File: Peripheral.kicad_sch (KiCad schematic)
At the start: 3 parts, among them U2 AT24CS02-XHM, U3 ICM-20602, U4 TJA1051T

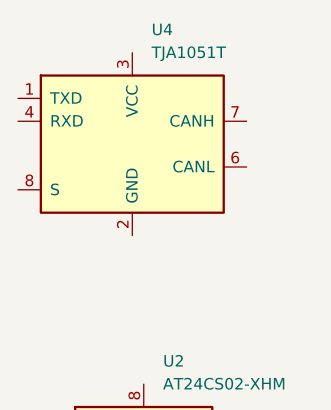
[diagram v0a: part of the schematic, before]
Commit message: 增加ADC采样，优化PWM
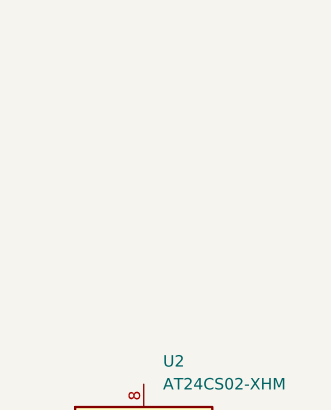
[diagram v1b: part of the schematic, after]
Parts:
- removed U4: TJA1051T, Package_SO:SOIC-8_3.9x4.9mm_P1.27mm, symbol Interface_CAN_LIN:TJA1051T
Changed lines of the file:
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@@
-	)
-	(symbol
-		(lib_id "Interface_CAN_LIN:TJA1051T")
-		(at 74.93 57.15 0)
-		(unit 1)
-		(exclude_from_sim no)
-		(in_bom yes)
-		(on_board yes)
-		(dnp no)
-		(fields_autoplaced yes)
-		(property "Reference" "U4"
-			(at 77.0733 44.45 0)
-			(effects
-				(font
-					(size 1.27 1.27)
-				)
-				(justify left)
-			)
-		)
-		(property "Value" "TJA1051T"
-			(at 77.0733 46.99 0)
-			(effects
-				(font
-					(size 1.27 1.27)
-				)
-				(justify left)
-			)
-		)
-		(property "Footprint" "Package_SO:SOIC-8_3.9x4.9mm_P1.27mm"
-			(at 74.93 69.85 0)
-			(effects
-				(font
-					(size 1.27 1.27)
-					(italic yes)
-				)
-				(hide yes)
-			)
-		)
-		(property "Datasheet" "http://www.nxp.com/docs/en/data-sheet/TJA1051.pdf"
-			(at 74.93 57.15 0)
-			(effects
-				(font
-					(size 1.27 1.27)
-				)
-				(hide yes)
-			)
-		)
-		(property "Description" "High-Speed CAN Transceiver, silent mode, SOIC-8"
-			(at 74.93 57.15 0)
-			(effects
-				(font
-					(size 1.27 1.27)
-				)
-				(hide yes)
-			)
-		)
-		(pin "6"
-		)
-		(pin "2"
-		)
-		(pin "1"
-		)
-		(pin "4"
-		)
-		(pin "5"
-		)
-		(pin "3"
-		)
-		(pin "8"
-		)
-		(pin "7"
-		)
-		(instances
-			(project "ControlBoard"
-				(path "/bfd4cee4-1f26-4ec9-a630-f44d434f4dbf/abd141e4-a687-4ce0-a8e9-dc522ad2ef55/5828d2be-30cc-492b-81f0-4c9eb7634256"
-					(reference "U4")
-					(unit 1)
-				)
-			)
-		)
 	)
 	(symbol

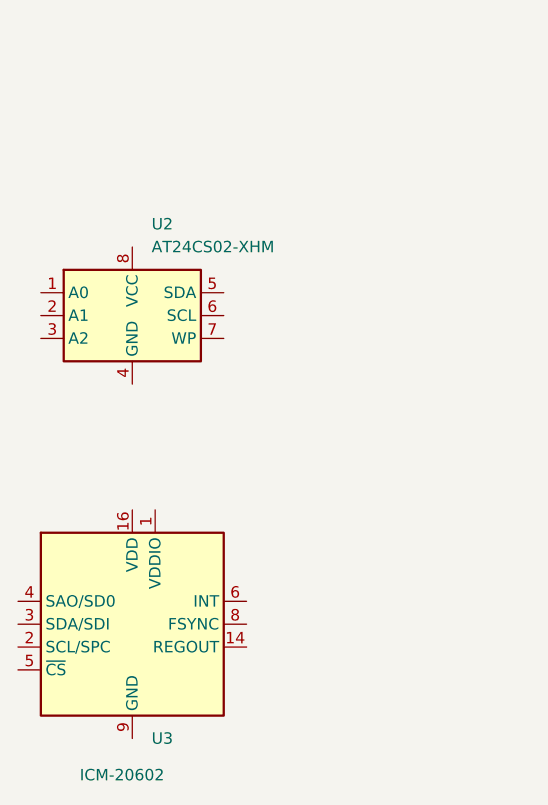
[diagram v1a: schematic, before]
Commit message: 完成部分I2C/FDCAN引脚分配
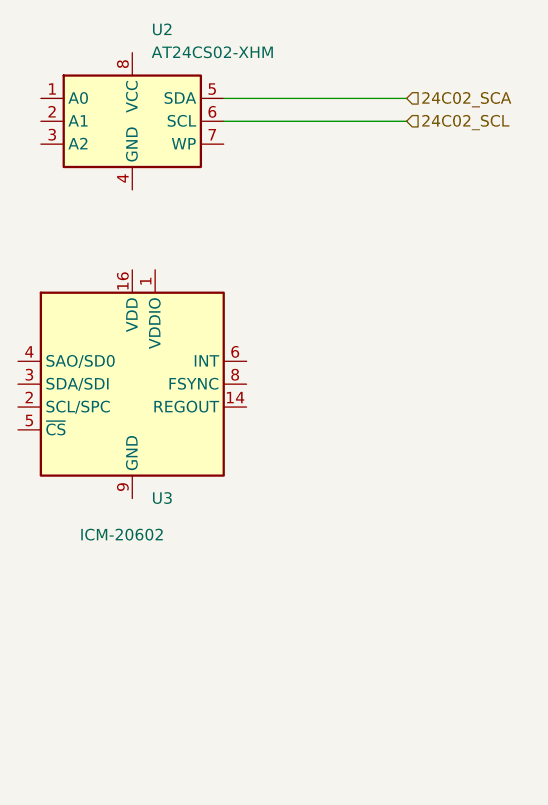
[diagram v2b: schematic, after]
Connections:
- net 24C02_SCA: now reaches U2.5 (SDA)
- net 24C02_SCL: now reaches U2.6 (SCL)
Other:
- moved on the sheet: U2, U3
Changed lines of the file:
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@@
 	(generator_version "9.0")
 	(paper "A4")
+	(wire
+		(pts
+			(xy 86.36 69.85) (xy 106.68 69.85)
+		)
+		(stroke
+			(width 0)
+			(type default)
+		)
+	)
+	(wire
+		(pts
+			(xy 86.36 67.31) (xy 106.68 67.31)
+		)
+		(stroke
+			(width 0)
+			(type default)
+		)
+	)
+	(hierarchical_label "24C02_SCL"
+		(shape input)
+		(at 106.68 69.85 0)
+		(effects
+			(font
+				(size 1.27 1.27)
+			)
+			(justify left)
+		)
+	)
+	(hierarchical_label "24C02_SCA"
+		(shape input)
+		(at 106.68 67.31 0)
+		(effects
+			(font
+				(size 1.27 1.27)
+			)
+			(justify left)
+		)
+	)
 	(symbol
 		(lib_id "Memory_EEPROM:AT24CS02-XHM")
-		(at 76.2 91.44 0)
+		(at 76.2 69.85 0)
 		(unit 1)
 		(exclude_from_sim no)
@@
 		(fields_autoplaced yes)
 		(property "Reference" "U2"
-			(at 78.3433 81.28 0)
+			(at 78.3433 59.69 0)
 			(effects
 				(font
@@
 		)
 		(property "Value" "AT24CS02-XHM"
-			(at 78.3433 83.82 0)
+			(at 78.3433 62.23 0)
 			(effects
 				(font
@@
 		)
 		(property "Footprint" "Package_SO:TSSOP-8_4.4x3mm_P0.65mm"
-			(at 76.2 91.44 0)
+			(at 76.2 69.85 0)
 			(effects
 				(font
@@
 		)
 		(property "Datasheet" "http://ww1.microchip.com/downloads/en/DeviceDoc/Atmel-8815-SEEPROM-AT24CS01-02-Datasheet.pdf"
-			(at 76.2 91.44 0)
+			(at 76.2 69.85 0)
 			(effects
 				(font
@@
 		)
 		(property "Description" "I2C Serial EEPROM, 2Kb (256x8) with Unique Serial Number, TSSOP8"
-			(at 76.2 91.44 0)
+			(at 76.2 69.85 0)
 			(effects
 				(font
@@
 	(symbol
 		(lib_id "Sensor_Motion:ICM-20602")
-		(at 76.2 125.73 0)
+		(at 76.2 99.06 0)
 		(unit 1)
 		(exclude_from_sim no)
@@
 		(dnp no)
 		(property "Reference" "U3"
-			(at 78.3433 138.43 0)
+			(at 78.3433 111.76 0)
 			(effects
 				(font
@@
 		)
 		(property "Value" "ICM-20602"
-			(at 70.358 142.494 0)
+			(at 70.358 115.824 0)
 			(effects
 				(font
@@
 		)
 		(property "Footprint" "Package_LGA:LGA-16_3x3mm_P0.5mm_LayoutBorder3x5y"
-			(at 76.2 119.38 0)
+			(at 76.2 92.71 0)
 			(effects
 				(font
@@
 		)
 		(property "Datasheet" "http://www.invensense.com/wp-content/uploads/2016/10/DS-000176-ICM-20602-v1.0.pdf"
-			(at 77.47 101.6 0)
+			(at 77.47 74.93 0)
 			(effects
 				(font
@@
 		)
 		(property "Description" "High performance 6-Axis MEMS motion tracking, SPI/I2C interface, LGA-16"
-			(at 76.2 125.73 0)
+			(at 76.2 99.06 0)
 			(effects
 				(font

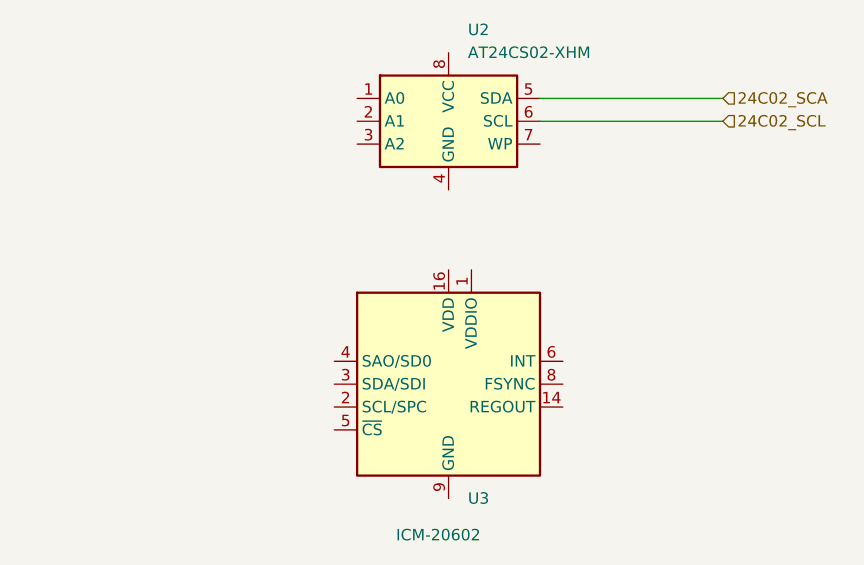
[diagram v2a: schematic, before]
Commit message: 增加3.3V电路
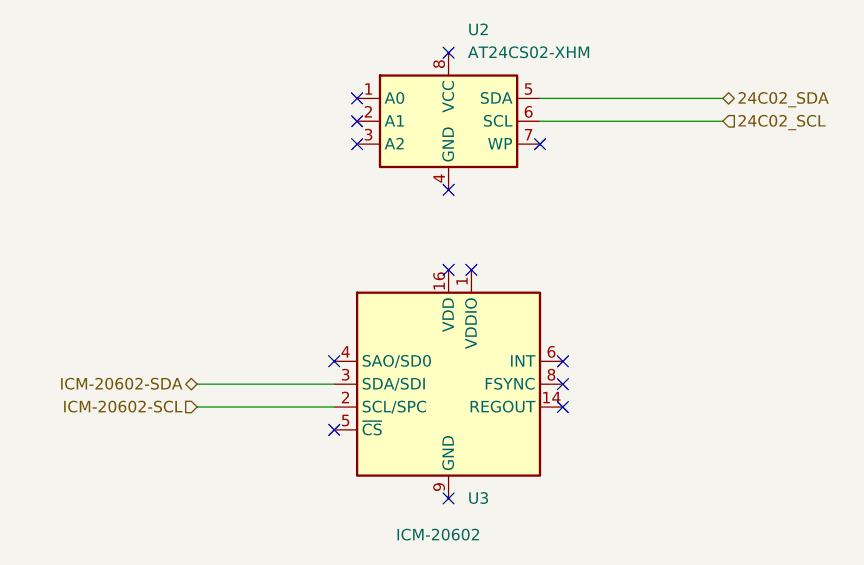
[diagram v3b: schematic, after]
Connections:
- net ICM-20602-SCL: now reaches U3.2 (SCL/SPC)
- net ICM-20602-SDA: now reaches U3.3 (SDA/SDI)
- net 24C02_SCA renamed 24C02_SDA
- no-connect marks 0 -> 14
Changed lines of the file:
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@@
 	(generator_version "9.0")
 	(paper "A4")
+	(no_connect
+		(at 63.5 96.52)
+	)
+	(no_connect
+		(at 88.9 99.06)
+	)
+	(no_connect
+		(at 66.04 72.39)
+	)
+	(no_connect
+		(at 78.74 86.36)
+	)
+	(no_connect
+		(at 63.5 104.14)
+	)
+	(no_connect
+		(at 66.04 67.31)
+	)
+	(no_connect
+		(at 88.9 101.6)
+	)
+	(no_connect
+		(at 88.9 96.52)
+	)
+	(no_connect
+		(at 66.04 69.85)
+	)
+	(no_connect
+		(at 86.36 72.39)
+	)
+	(no_connect
+		(at 76.2 111.76)
+	)
+	(no_connect
+		(at 76.2 62.23)
+	)
+	(no_connect
+		(at 76.2 77.47)
+	)
+	(no_connect
+		(at 76.2 86.36)
+	)
+	(wire
+		(pts
+			(xy 48.26 99.06) (xy 63.5 99.06)
+		)
+		(stroke
+			(width 0)
+			(type default)
+		)
+	)
+	(wire
+		(pts
+			(xy 48.26 101.6) (xy 63.5 101.6)
+		)
+		(stroke
+			(width 0)
+			(type default)
+		)
+	)
 	(wire
 		(pts
@@
 		)
 	)
+	(hierarchical_label "ICM-20602-SDA"
+		(shape bidirectional)
+		(at 48.26 99.06 180)
+		(effects
+			(font
+				(size 1.27 1.27)
+			)
+			(justify right)
+		)
+	)
 	(hierarchical_label "24C02_SCL"
 		(shape input)
@@
 		)
 	)
-	(hierarchical_label "24C02_SCA"
-		(shape input)
+	(hierarchical_label "24C02_SDA"
+		(shape bidirectional)
 		(at 106.68 67.31 0)
 		(effects
@@
 		)
 	)
+	(hierarchical_label "ICM-20602-SCL"
+		(shape input)
+		(at 48.26 101.6 180)
+		(effects
+			(font
+				(size 1.27 1.27)
+			)
+			(justify right)
+		)
+	)

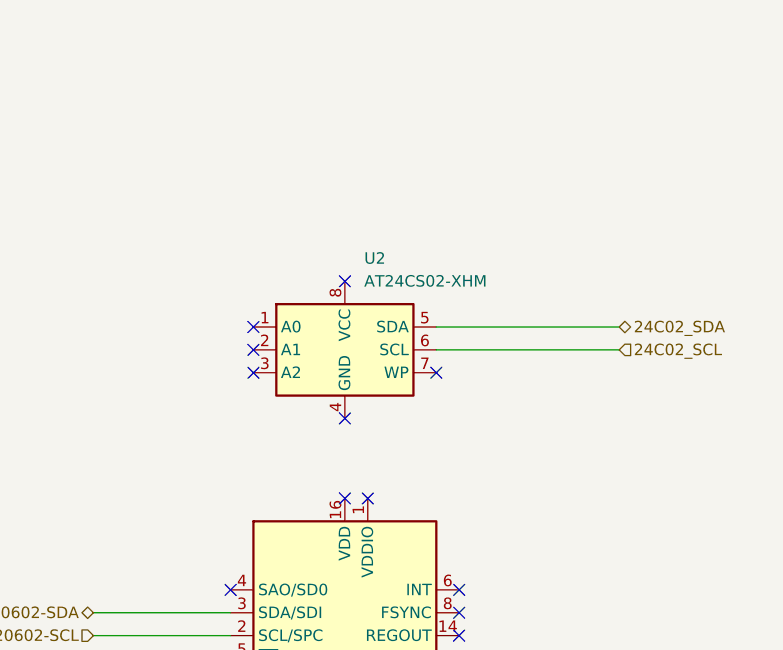
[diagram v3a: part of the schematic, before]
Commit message: 优化EEPROM电路
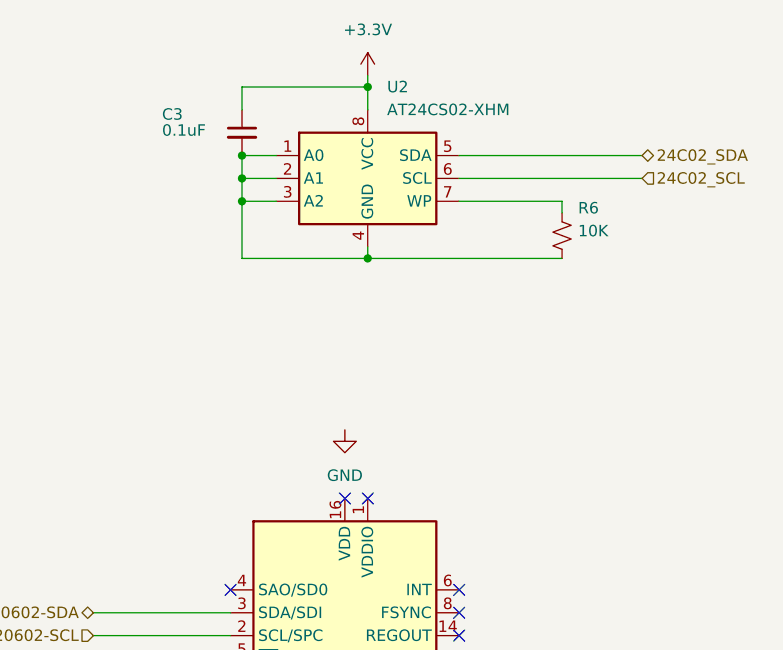
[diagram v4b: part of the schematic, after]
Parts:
- added C3: 0.1uF, symbol Device:C_Small
- added R6: 10K, symbol Device:R_Small_US
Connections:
- net at U2.1 (A0): now also U2.2 (A1), U2.3 (A2), U2.4 (GND), C3.2, R6.2
- net at U2.7 (WP): now also R6.1
- net +3.3V: now reaches U2.8 (VCC)
- net +3.3V: now also C3.1
- no-connect marks 14 -> 8
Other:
- moved on the sheet: U2

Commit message: 优化IMU电路
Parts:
- added U6: ICM-4268-P, Package_LGA:Bosch_LGA-14_3x2.5mm_P0.5mm, symbol User_Driver:ICM-42688-P
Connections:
- net GND: now also C3.2, R6.2, U2.1 (A0), U2.2 (A1), U2.3 (A2), U2.4 (GND)
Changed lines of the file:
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@@
 	(symbol
 		(lib_id "power:GND")
-		(at 76.2 78.74 0)
+		(at 78.74 59.69 0)
 		(unit 1)
 		(exclude_from_sim no)
@@
 		(fields_autoplaced yes)
 		(property "Reference" "#PWR012"
-			(at 76.2 85.09 0)
+			(at 78.74 66.04 0)
 			(effects
 				(font
@@
 		)
 		(property "Value" "GND"
-			(at 76.2 83.82 0)
+			(at 78.74 64.77 0)
 			(effects
 				(font
@@
 		)
 		(property "Footprint" ""
-			(at 76.2 78.74 0)
+			(at 78.74 59.69 0)
 			(effects
 				(font
@@
 		)
 		(property "Datasheet" ""
-			(at 76.2 78.74 0)
+			(at 78.74 59.69 0)
 			(effects
 				(font
@@
 		)
 		(property "Description" "Power symbol creates a global label with name \"GND\" , ground"
-			(at 76.2 78.74 0)
+			(at 78.74 59.69 0)
 			(effects
 				(font
@@
 					(unit 1)
 				)
+			)
+		)
+	)
+	(symbol
+		(lib_id "User_Driver:ICM-42688-P")
+		(at 113.03 85.09 0)
+		(unit 1)
+		(exclude_from_sim no)
+		(in_bom yes)
+		(on_board yes)
+		(dnp no)
+		(fields_autoplaced yes)
+		(property "Reference" "U6"
+			(at 129.54 80.01 0)
+			(effects
+				(font
+					(size 1.27 1.27)
+				)
+			)
+		)
+		(property "Value" "ICM-4268-P"
+			(at 129.54 82.55 0)
+			(effects
+				(font
+					(size 1.27 1.27)
+				)
+			)
+		)
+		(property "Footprint" "Package_LGA:Bosch_LGA-14_3x2.5mm_P0.5mm"
+			(at 113.03 85.09 0)
+			(effects
+				(font
+					(size 1.27 1.27)
+				)
+				(hide yes)
+			)
+		)
+		(property "Datasheet" ""
+			(at 113.03 85.09 0)
+			(effects
+				(font
+					(size 1.27 1.27)
+				)
+				(hide yes)
+			)
+		)
+		(property "Description" ""
+			(at 113.03 85.09 0)
+			(effects
+				(font
+					(size 1.27 1.27)
+				)
+				(hide yes)
+			)
+		)
+		(pin "6"
+		)
+		(pin "9"
+		)
+		(pin "11"
+		)
+		(pin "1"
+		)
+		(pin "5"
+		)
+		(pin "10"
+		)
+		(pin "2"
+		)
+		(pin "7"
+		)
+		(pin "12"
+		)
+		(pin "8"
+		)
+		(pin "14"
+		)
+		(pin "3"
+		)
+		(pin "4"
+		)
+		(pin "13"
+		)
+		(instances
+			(project ""
+				(path "/bfd4cee4-1f26-4ec9-a630-f44d434f4dbf/abd141e4-a687-4ce0-a8e9-dc522ad2ef55/5828d2be-30cc-492b-81f0-4c9eb7634256"
+					(reference "U6")
+					(unit 1)
+				)

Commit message: 优化IMU电路
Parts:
- removed U3: ICM-20602, Package_LGA:LGA-16_3x3mm_P0.5mm_LayoutBorder3x5y, symbol Sensor_Motion:ICM-20602
- removed U6: ICM-4268-P, Package_LGA:Bosch_LGA-14_3x2.5mm_P0.5mm, symbol User_Driver:ICM-42688-P
- added C4: 0.1uF, symbol Device:C_Small
- added C5: 2.2uF, symbol Device:C_Small
- added C6: 0.01uF, symbol Device:C_Small
- added R7, R8: 10K, symbol Device:R_Small_US
- added U3: ICM-4268-P, Package_LGA:Bosch_LGA-14_3x2.5mm_P0.5mm, symbol User_Driver:ICM-42688-P
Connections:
- net +3.3V: now also C4.1, C5.1, C6.1, R7.1, U3.5 (VDDIO), U3.8 (VDD)
- net GND: now also C4.2, C5.2, C6.2, R8.2, U3.10 (RESV), U3.11 (RESV), U3.2 (RESV), U3.3 (RESV), U3.6 (GND), U3.7 (RESV)
- net ICM-20602-SCL: now also U3.13 (AP_SCL/AP_SCLK)
- net ICM-20602-SDA: now also U3.14 (AP_SDA/AP_SDIO/AP_SDI)
- new net: R8.1, U3.9 (INT2/FSYNC/CLKIN)
- new net: R7.2, U3.1 (AP_SDO/AP_SD0), U3.12 (AP_CS)
- new net ICM-20602-INT: U3.4 (INT1/INT)
- no-connect marks 8 -> 0
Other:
- note added: "EEPROM"
- note added: "IMU"
- moved on the sheet: C3, R6, U2

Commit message: 优化接口
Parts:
- added C10, C9: 0.1uF, Capacitor_SMD:C_0603_1608Metric_Pad1.08x0.95mm_HandSolder, symbol Device:C_Small
- added C7, C8: 100pF, Capacitor_SMD:C_0603_1608Metric_Pad1.08x0.95mm_HandSolder, symbol Device:C_Small
- added R10, R11: 10R, Resistor_SMD:R_0603_1608Metric_Pad0.98x0.95mm_HandSolder, symbol Device:R_Small_US
- added R12: 120R, Resistor_SMD:R_0603_1608Metric_Pad0.98x0.95mm_HandSolder, symbol Device:R_Small_US
- added R4: 0R, Resistor_SMD:R_0603_1608Metric_Pad0.98x0.95mm_HandSolder, symbol Device:R_Small_US
- added U6: TLE9251VSJ, Package_SO:Infineon_PG-DSO-8-24_4x5mm, symbol User_Driver:TLE9251VSJ
- C3, C4, C5, C6: footprint (none) -> Capacitor_SMD:C_0603_1608Metric_Pad1.08x0.95mm_HandSolder
- R6, R7, R8: footprint (none) -> Resistor_SMD:R_0603_1608Metric_Pad0.98x0.95mm_HandSolder
- U3: value ICM-4268-P -> ICM-42668-P
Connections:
- net +3.3V: now also C9.1, U6.5 (VIO)
- net GND: now also C10.2, C7.2, C8.2, C9.2, R4.1, U6.2 (GND)
- new net: R11.1, U6.6 (CAN_L)
- new net: R10.1, U6.7 (CAN_H)
- new net: R4.2, U6.8 (STB)
- new net +5V: C10.1, U6.3 (VCC)
- new net PB11_FDCAN2_RX: C7.1, U6.4 (RXD)
- new net PB6_FDCAN2_TX: C8.1, U6.1 (TXD)
- new net TLE9251VSJ_H: R10.2, R12.1
- new net TLE9251VSJ_L: R11.2, R12.2
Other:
- note added: "CAN"
- moved on the sheet: C3, R6, U2
